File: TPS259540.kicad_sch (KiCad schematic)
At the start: 20 parts, among them Q5 2N7002, U5 TPS259540DSGR

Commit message: Cleaned up schematic and replaced TC358743XBG with reverse-engineered LT6911C
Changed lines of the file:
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@@
+		)
+	)
+	(hierarchical_label "+3V3"
+		(shape input)
+		(at 160.02 73.66 0)
+		(effects
+			(font
+				(size 1.27 1.27)
+			)
+			(justify left)
+		)
+	)
+	(hierarchical_label "+3V3"
+		(shape input)
+		(at 0.3048 0.8096 0)
+		(effects
+			(font
+				(size 1.27 1.27)
+			)
+			(justify left)
 		)
 	)
@@
 		(shape input)
 		(at 57.15 55.88 180)
+		(effects
+			(font
+				(size 1.27 1.27)
+			)
+			(justify right)
+		)
+	)
+	(hierarchical_label "GND"
+		(shape input)
+		(at 57.15 80.01 180)
 		(effects
 			(font
@@
 					(unit 1)
 				)
-			)
-		)
-	)
-	(symbol
-		(lib_id "power:+1V1")
-		(at 160.02 73.66 0)
-		(unit 1)
-		(body_style 1)
-		(exclude_from_sim no)
-		(in_bom yes)
-		(on_board yes)
-		(in_pos_files yes)
-		(dnp no)
-		(property "Reference" "#PWR047"
-			(at 160.02 77.47 0)
-			(hide yes)
-			(show_name no)
-			(do_not_autoplace no)
-			(effects
-				(font
-					(size 1.27 1.27)
-				)
-			)
-		)
-		(property "Value" "+3V3"
-			(at 155.956 71.882 0)
-			(show_name no)
-			(do_not_autoplace no)
-			(effects
-				(font
-					(size 1.27 1.27)
-				)
-			)
-		)
-		(property "Footprint" ""
-			(at 160.02 73.66 0)
-			(hide yes)
-			(show_name no)
-			(do_not_autoplace no)
-			(effects
-				(font
-					(size 1.27 1.27)
-				)
-			)
-		)
-		(property "Datasheet" ""
-			(at 160.02 73.66 0)
-			(hide yes)
-			(show_name no)
-			(do_not_autoplace no)
-			(effects
-				(font
-					(size 1.27 1.27)
-				)
-			)
-		)
-		(property "Description" "Power symbol creates a global label with name \"+1V1\""
-			(at 160.02 73.66 0)
-			(hide yes)
-			(show_name no)
-			(do_not_autoplace no)
-			(effects
-				(font
-					(size 1.27 1.27)
-				)
-			)
-		)
-		(pin "1"
-		)
-		(instances
-			(project "serverv2_backplane"
-				(path "/d38d6818-cf53-410d-afa3-a75a85b7c05a/1271a149-7432-404a-bbd5-7ae0b7a8d68d/aa340d7a-66d0-4862-ab8a-34395ba33866"
-					(reference "#PWR0905")
-					(unit 1)
-				)
-				(path "/d38d6818-cf53-410d-afa3-a75a85b7c05a/2b34bdfe-333e-4210-8353-2d6d8e14690a/aa340d7a-66d0-4862-ab8a-34395ba33866"
-					(reference "#PWR0743")
-					(unit 1)
-				)
-				(path "/d38d6818-cf53-410d-afa3-a75a85b7c05a/2b409005-8f0c-424d-bea3-7f99170f3949/aa340d7a-66d0-4862-ab8a-34395ba33866"
-					(reference "#PWR0635")
-					(unit 1)
-				)
-				(path "/d38d6818-cf53-410d-afa3-a75a85b7c05a/46262d05-a782-4c24-8fee-232f080edae1/aa340d7a-66d0-4862-ab8a-34395ba33866"
-					(reference "#PWR0695")
-					(unit 1)
-				)
-				(path "/d38d6818-cf53-410d-afa3-a75a85b7c05a/470b220a-a565-4e43-ab90-9eb03ea2cd43/aa340d7a-66d0-4862-ab8a-34395ba33866"
-					(reference "#PWR0563")
-					(unit 1)
-				)
-				(path "/d38d6818-cf53-410d-afa3-a75a85b7c05a/4cfb14a9-2f19-498b-8efa-0b74e4ca5f47/aa340d7a-66d0-4862-ab8a-34395ba33866"
-					(reference "#PWR047")
-					(unit 1)
-				)
-				(path "/d38d6818-cf53-410d-afa3-a75a85b7c05a/50af50d7-94b3-4b11-b0b0-fb1dfb06c699/aa340d7a-66d0-4862-ab8a-34395ba33866"
-					(reference "#PWR0862")
-					(unit 1)
-				)
-				(path "/d38d6818-cf53-410d-afa3-a75a85b7c05a/8533a259-5737-4fce-b4c0-279539c49b16/aa340d7a-66d0-4862-ab8a-34395ba33866"
-					(reference "#PWR0948")
-					(unit 1)
-				)
-				(path "/d38d6818-cf53-410d-afa3-a75a85b7c05a/a91f2db0-df6c-4013-b7b0-c2c51c5a6ec1/aa340d7a-66d0-4862-ab8a-34395ba33866"
-					(reference "#PWR0597")
-					(unit 1)
-				)
-				(path "/d38d6818-cf53-410d-afa3-a75a85b7c05a/bfbdef84-70db-44df-9f2c-b3e154a7a6cb/aa340d7a-66d0-4862-ab8a-34395ba33866"
-					(reference "#PWR0515")
-					(unit 1)
-				)
-				(path "/d38d6818-cf53-410d-afa3-a75a85b7c05a/c1d5cf6d-a75d-4df1-9c1d-6d5e2a990df7/aa340d7a-66d0-4862-ab8a-34395ba33866"
-					(reference "#PWR0791")
-					(unit 1)
-				)
-				(path "/d38d6818-cf53-410d-afa3-a75a85b7c05a/ca25108c-b61e-40df-845b-d107b2a6dbc6/aa340d7a-66d0-4862-ab8a-34395ba33866"
-					(reference "#PWR0996")
-					(unit 1)
-				)

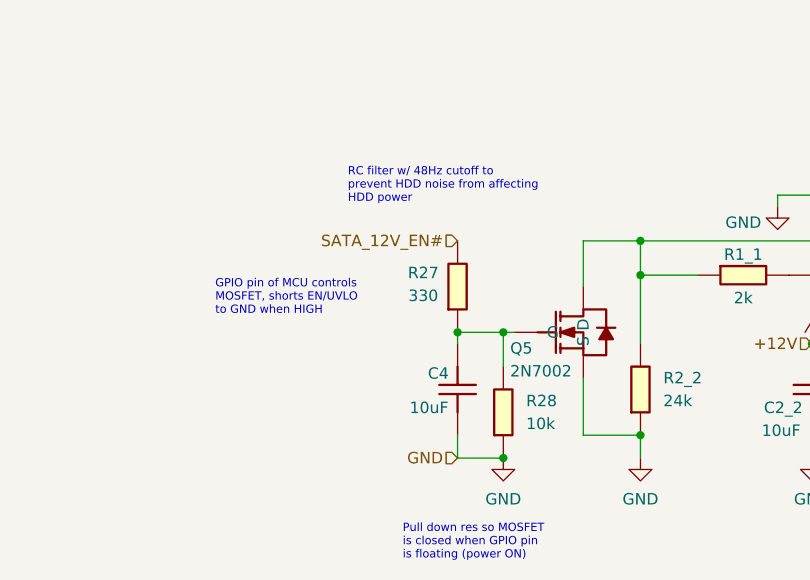
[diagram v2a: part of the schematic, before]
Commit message: Basic Function Review/Documentation for LT6911C Subsystem
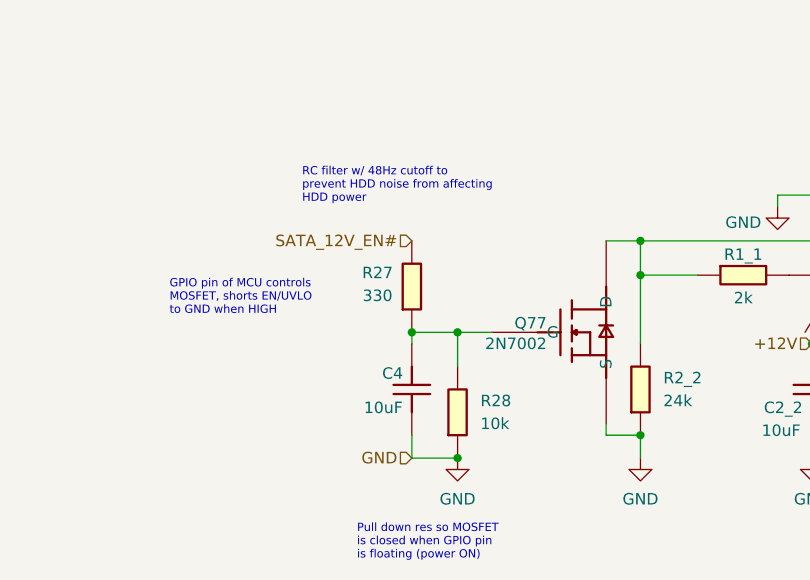
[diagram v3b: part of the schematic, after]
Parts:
- removed Q5: 2N7002, Package_TO_SOT_SMD:SOT-23-3, symbol JLCImport:2N7002
- added Q77: 2N7002, JLCImport:2N7002_C916396, symbol JLCImport:2N7002_C916396
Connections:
- net GND: now also Q77.2 (S)
- net at C4.2, R27.1, R28.2: now also Q77.1 (G)
- net at R1_1.1, R2_2.2, U5.2 (EN/UVLO): now also Q77.3 (D)
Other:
- moved on the sheet: C4, R27, R28
